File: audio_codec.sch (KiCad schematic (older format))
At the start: 9 parts, among them J5 AudioJack3, U5 TLV320AIC23BRHD, Y2 AUDIO_CLK

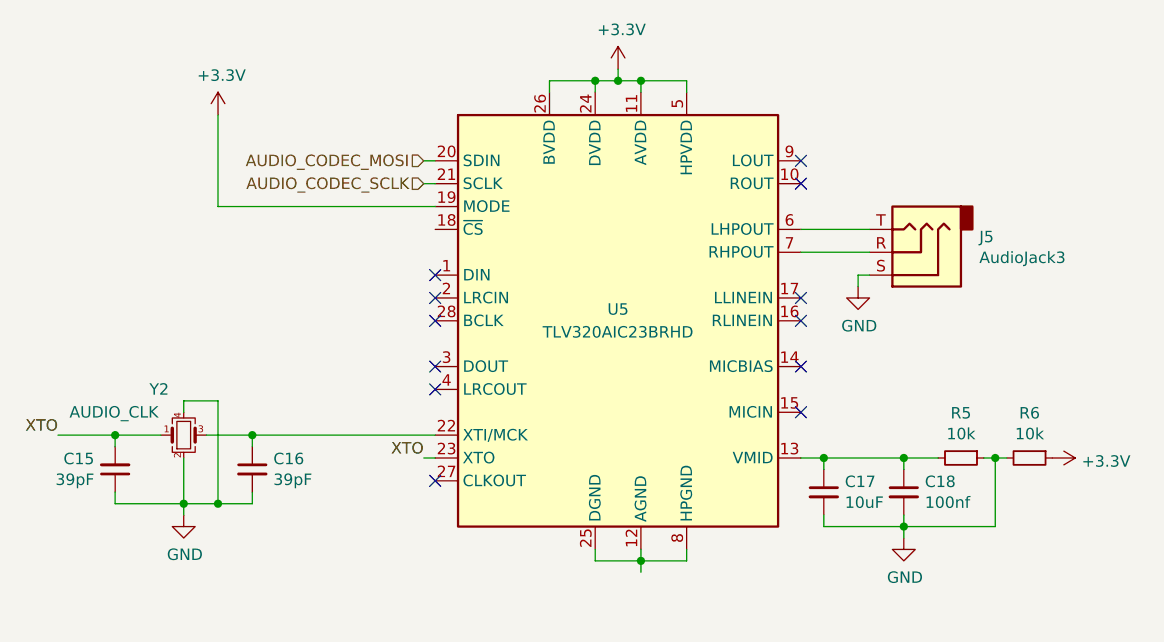
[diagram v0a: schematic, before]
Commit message: Updated footprints
Updated some parts to JLCPCB SMT library and also added some footprints
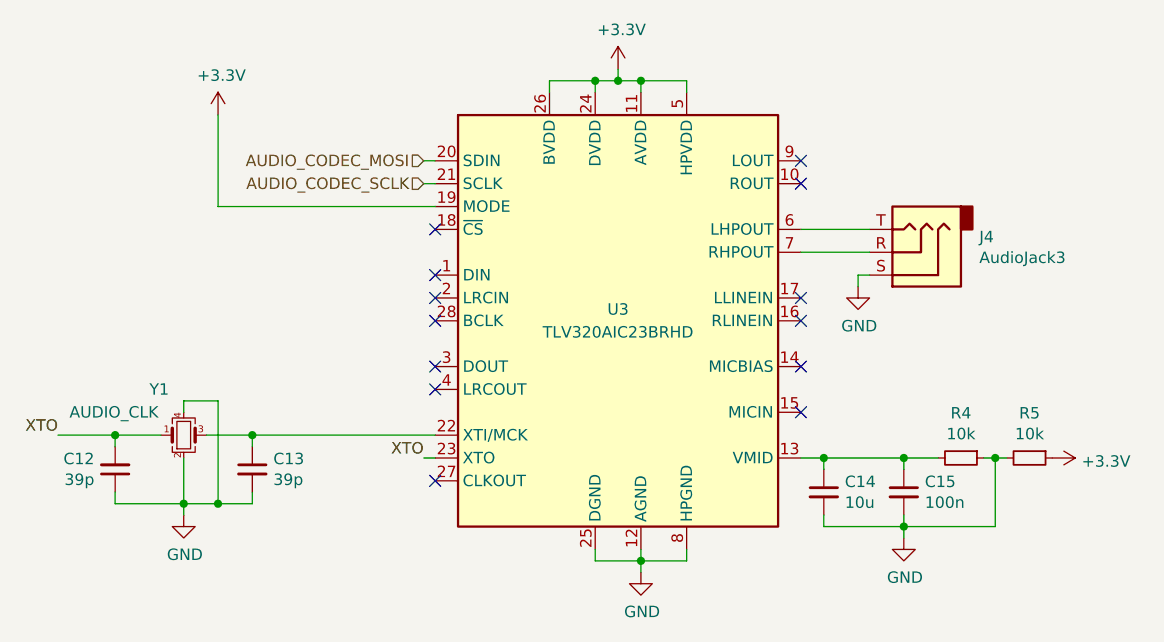
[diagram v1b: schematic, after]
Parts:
- C12: renamed from C15; value 39pF -> 39p; footprint (none) -> Capacitor_SMD:C_0603_1608Metric
- C13: renamed from C16; value 39pF -> 39p; footprint (none) -> Capacitor_SMD:C_0603_1608Metric
- C14: renamed from C17; value 10uF -> 10u; footprint (none) -> Capacitor_SMD:C_0805_2012Metric
- C15: renamed from C18; value 100nf -> 100n; footprint (none) -> Capacitor_SMD:C_0402_1005Metric
- J4: renamed from J5; footprint (none) -> Connector_Audio:Jack_3.5mm_CUI_SJ-3523-SMT_Horizontal
- renumbered R5 to R4, R6 to R5, U5 to U3, Y2 to Y1
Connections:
- net GND: now also U3.12 (AGND), U3.25 (DGND), U3.29 (AGND), U3.8 (HPGND)
- no-connect marks 12 -> 13
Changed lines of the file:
@@
 $Descr A4 11693 8268
 encoding utf-8
-Sheet 3 4
+Sheet 2 4
 Title "MP3 Player"
 Date "2021-02-28"
@@
 $EndDescr
 $Comp
-L Audio:TLV320AIC23BRHD U5
+L Audio:TLV320AIC23BRHD U3
 U 1 1 60D43EB3
 P 5800 3950
-F 0 "U5" H 5800 4000 50  0000 C CNN
+F 0 "U3" H 5800 4000 50  0000 C CNN
 F 1 "TLV320AIC23BRHD" H 5800 3900 50  0000 C CNN
 F 2 "Package_DFN_QFN:QFN-28-1EP_5x5mm_P0.5mm_EP3.35x3.35mm" H 5800 3950 50  0001 C CIN
@@
 NoConn ~ 6600 3950
 $Comp
-L Connector:AudioJack3 J5
+L Connector:AudioJack3 J4
 U 1 1 60D43EC2
 P 7100 3650
-F 0 "J5" H 6820 3583 50  0000 R CNN
+F 0 "J4" H 6820 3583 50  0000 R CNN
 F 1 "AudioJack3" H 6820 3674 50  0000 R CNN
-F 2 "" H 7100 3650 50  0001 C CNN
+F 2 "Connector_Audio:Jack_3.5mm_CUI_SJ-3523-SMT_Horizontal" H 7100 3650 50  0001 C CNN
 F 3 "~" H 7100 3650 50  0001 C CNN
 	1    7100 3650
@@
 	4950 3350 5000 3350
 $Comp
-L power:+3.3V #PWR0121
+L power:+3.3V #PWR013
 U 1 1 60D43ECD
 P 4050 3050
-F 0 "#PWR0121" H 4050 2900 50  0001 C CNN
+F 0 "#PWR013" H 4050 2900 50  0001 C CNN
 F 1 "+3.3V" H 4065 3223 50  0000 C CNN
 F 2 "" H 4050 3050 50  0001 C CNN
@@
 NoConn ~ 5000 4250
 $Comp
-L power:+3.3V #PWR0122
+L power:+3.3V #PWR018
 U 1 1 60D43EDA
 P 7700 4550
-F 0 "#PWR0122" H 7700 4400 50  0001 C CNN
+F 0 "#PWR018" H 7700 4400 50  0001 C CNN
 F 1 "+3.3V" V 7715 4678 50  0000 L CNN
 F 2 "" H 7700 4550 50  0001 C CNN
@@
 $EndComp
 $Comp
-L Device:R_Small R6
+L Device:R_Small R5
 U 1 1 60D43EE0
 P 7600 4550
-F 0 "R6" V 7404 4550 50  0000 C CNN
+F 0 "R5" V 7404 4550 50  0000 C CNN
 F 1 "10k" V 7495 4550 50  0000 C CNN
 F 2 "" H 7600 4550 50  0001 C CNN
@@
 $EndComp
 $Comp
-L Device:R_Small R5
+L Device:R_Small R4
 U 1 1 60D43EE6
 P 7300 4550
-F 0 "R5" V 7104 4550 50  0000 C CNN
+F 0 "R4" V 7104 4550 50  0000 C CNN
 F 1 "10k" V 7195 4550 50  0000 C CNN
 F 2 "" H 7300 4550 50  0001 C CNN
@@
 $EndComp
 $Comp
-L Device:C_Small C17
+L Device:C_Small C14
 U 1 1 60D43EEC
 P 6700 4700
-F 0 "C17" H 6792 4746 50  0000 L CNN
-F 1 "10uF" H 6792 4655 50  0000 L CNN
-F 2 "" H 6700 4700 50  0001 C CNN
+F 0 "C14" H 6792 4746 50  0000 L CNN
+F 1 "10u" H 6792 4655 50  0000 L CNN
+F 2 "Capacitor_SMD:C_0805_2012Metric" H 6700 4700 50  0001 C CNN
 F 3 "~" H 6700 4700 50  0001 C CNN
 	1    6700 4700
@@
 $EndComp
 $Comp
-L Device:C_Small C18
+L Device:C_Small C15
 U 1 1 60D43EF2
 P 7050 4700
-F 0 "C18" H 7142 4746 50  0000 L CNN
-F 1 "100nf" H 7142 4655 50  0000 L CNN
-F 2 "" H 7050 4700 50  0001 C CNN
+F 0 "C15" H 7142 4746 50  0000 L CNN
+F 1 "100n" H 7142 4655 50  0000 L CNN
+F 2 "Capacitor_SMD:C_0402_1005Metric" H 7050 4700 50  0001 C CNN
 F 3 "~" H 7050 4700 50  0001 C CNN
 	1    7050 4700
@@
 	7050 4550 6700 4550
 $Comp
-L power:GND #PWR0123
+L power:GND #PWR017
 U 1 1 60D43EFF
 P 7050 4900
-F 0 "#PWR0123" H 7050 4650 50  0001 C CNN
+F 0 "#PWR017" H 7050 4650 50  0001 C CNN
 F 1 "GND" H 7055 4727 50  0000 C CNN
 F 2 "" H 7050 4900 50  0001 C CNN
@@
 Wire Wire Line
 	7450 4550 7500 4550
-$Comp
-L power:+3.3V #PWR0124
-U 1 1 60D43F0F
-P 5800 2850
-F 0 "#PWR0124" H 5800 2700 50  0001 C CNN
-F 1 "+3.3V" H 5815 3023 50  0000 C CNN
-F 2 "" H 5800 2850 50  0001 C CNN
-F 3 "" H 5800 2850 50  0001 C CNN
-	1    5800 2850
-	1    0    0    -1
-$EndComp
-Wire Wire Line
-	5500 2950 5500 2900
-Wire Wire Line
-	5500 2900 5700 2900
-Wire Wire Line
-	6100 2900 6100 2950
-Wire Wire Line
-	5800 2900 5800 2850
-Connection ~ 5800 2900
-Wire Wire Line
-	5800 2900 5900 2900
-Wire Wire Line
-	5700 2950 5700 2900
-Connection ~ 5700 2900
-Wire Wire Line
-	5700 2900 5800 2900
-Wire Wire Line
-	5900 2950 5900 2900
-Connection ~ 5900 2900
-Wire Wire Line
-	5900 2900 6100 2900
 NoConn ~ 5000 4650
 $Comp
-L Device:Crystal_GND24_Small Y2
+L Device:Crystal_GND24_Small Y1
 U 1 1 60D43F22
 P 3900 4450
-F 0 "Y2" H 3750 4650 50  0000 L CNN
+F 0 "Y1" H 3750 4650 50  0000 L CNN
 F 1 "AUDIO_CLK" H 3400 4550 50  0000 L CNN
 F 2 "" H 3900 4450 50  0001 C CNN
@@
 	4950 4550 5000 4550
 $Comp
-L Device:C_Small C15
+L Device:C_Small C12
 U 1 1 60D43F2C
 P 3600 4600
-F 0 "C15" H 3509 4554 50  0000 R CNN
-F 1 "39pF" H 3509 4645 50  0000 R CNN
-F 2 "" H 3600 4600 50  0001 C CNN
+F 0 "C12" H 3509 4554 50  0000 R CNN
+F 1 "39p" H 3509 4645 50  0000 R CNN
+F 2 "Capacitor_SMD:C_0603_1608Metric" H 3600 4600 50  0001 C CNN
 F 3 "~" H 3600 4600 50  0001 C CNN
 	1    3600 4600
@@
 $EndComp
 $Comp
-L Device:C_Small C16
+L Device:C_Small C13
 U 1 1 60D43F32
 P 4200 4600
-F 0 "C16" H 4292 4646 50  0000 L CNN
-F 1 "39pF" H 4292 4555 50  0000 L CNN
-F 2 "" H 4200 4600 50  0001 C CNN
+F 0 "C13" H 4292 4646 50  0000 L CNN
+F 1 "39p" H 4292 4555 50  0000 L CNN
+F 2 "Capacitor_SMD:C_0603_1608Metric" H 4200 4600 50  0001 C CNN
 F 3 "~" H 4200 4600 50  0001 C CNN
 	1    4200 4600
@@
 	3600 4450 3800 4450
 $Comp
-L power:GND #PWR0125
+L power:GND #PWR012
 U 1 1 60D43F3D
 P 3900 4800
-F 0 "#PWR0125" H 3900 4550 50  0001 C CNN
+F 0 "#PWR012" H 3900 4550 50  0001 C CNN
 F 1 "GND" H 3905 4627 50  0000 C CNN
 F 2 "" H 3900 4800 50  0001 C CNN
@@
 	4050 4750 4200 4750
 $Comp
-L power:GND #PWR0126
+L power:GND #PWR016
 U 1 1 60D43F54
 P 6850 3800
-F 0 "#PWR0126" H 6850 3550 50  0001 C CNN
+F 0 "#PWR016" H 6850 3550 50  0001 C CNN
 F 1 "GND" H 6855 3627 50  0000 C CNN
 F 2 "" H 6850 3800 50  0001 C CNN
@@
 Text HLabel 4950 3350 0    50   Input ~ 0
 AUDIO_CODEC_SCLK
+$Comp
+L power:GND #PWR015
+U 1 1 60F224AE
+P 5900 5050
+F 0 "#PWR015" H 5900 4800 50  0001 C CNN
+F 1 "GND" H 5905 4877 50  0000 C CNN
+F 2 "" H 5900 5050 50  0001 C CNN
+F 3 "" H 5900 5050 50  0001 C CNN
+	1    5900 5050
+	1    0    0    -1
+$EndComp
+NoConn ~ 5000 3550
+Wire Wire Line
+	6100 2900 6100 2950
+$Comp
+L power:+3.3V #PWR014
+U 1 1 60D43F0F
+P 5800 2850
+F 0 "#PWR014" H 5800 2700 50  0001 C CNN
+F 1 "+3.3V" H 5815 3023 50  0000 C CNN
+F 2 "" H 5800 2850 50  0001 C CNN
+F 3 "" H 5800 2850 50  0001 C CNN
+	1    5800 2850
+	1    0    0    -1
+$EndComp
+Wire Wire Line
+	5500 2950 5500 2900
+Wire Wire Line
+	5700 2900 5700 2950
+Wire Wire Line
+	5500 2900 5700 2900
+Connection ~ 5700 2900
+Wire Wire Line
+	5700 2900 5800 2900
+Wire Wire Line
+	5800 2900 5800 2850
+Connection ~ 5800 2900
+Wire Wire Line
+	5800 2900 5900 2900
+Wire Wire Line
+	5900 2900 6100 2900
+Connection ~ 5900 2900
+Wire Wire Line
+	5900 2950 5900 2900
 $EndSCHEMATC

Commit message: Update footprints
Add footprints for resistors, push buttons, regulator, and crystals
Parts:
- R4, R5: footprint (none) -> Resistor_SMD:R_1206_3216Metric
- Y1: footprint (none) -> Crystal:Crystal_SMD_3225-4Pin_3.2x2.5mm
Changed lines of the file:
@@
 F 0 "R5" V 7404 4550 50  0000 C CNN
 F 1 "10k" V 7495 4550 50  0000 C CNN
-F 2 "" H 7600 4550 50  0001 C CNN
+F 2 "Resistor_SMD:R_1206_3216Metric" H 7600 4550 50  0001 C CNN
 F 3 "~" H 7600 4550 50  0001 C CNN
 	1    7600 4550
@@
 F 0 "R4" V 7104 4550 50  0000 C CNN
 F 1 "10k" V 7195 4550 50  0000 C CNN
-F 2 "" H 7300 4550 50  0001 C CNN
+F 2 "Resistor_SMD:R_1206_3216Metric" H 7300 4550 50  0001 C CNN
 F 3 "~" H 7300 4550 50  0001 C CNN
 	1    7300 4550
@@
 F 0 "Y1" H 3750 4650 50  0000 L CNN
 F 1 "AUDIO_CLK" H 3400 4550 50  0000 L CNN
-F 2 "" H 3900 4450 50  0001 C CNN
+F 2 "Crystal:Crystal_SMD_3225-4Pin_3.2x2.5mm" H 3900 4450 50  0001 C CNN
 F 3 "~" H 3900 4450 50  0001 C CNN
 	1    3900 4450
